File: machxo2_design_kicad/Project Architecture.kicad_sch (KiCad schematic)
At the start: 0 parts

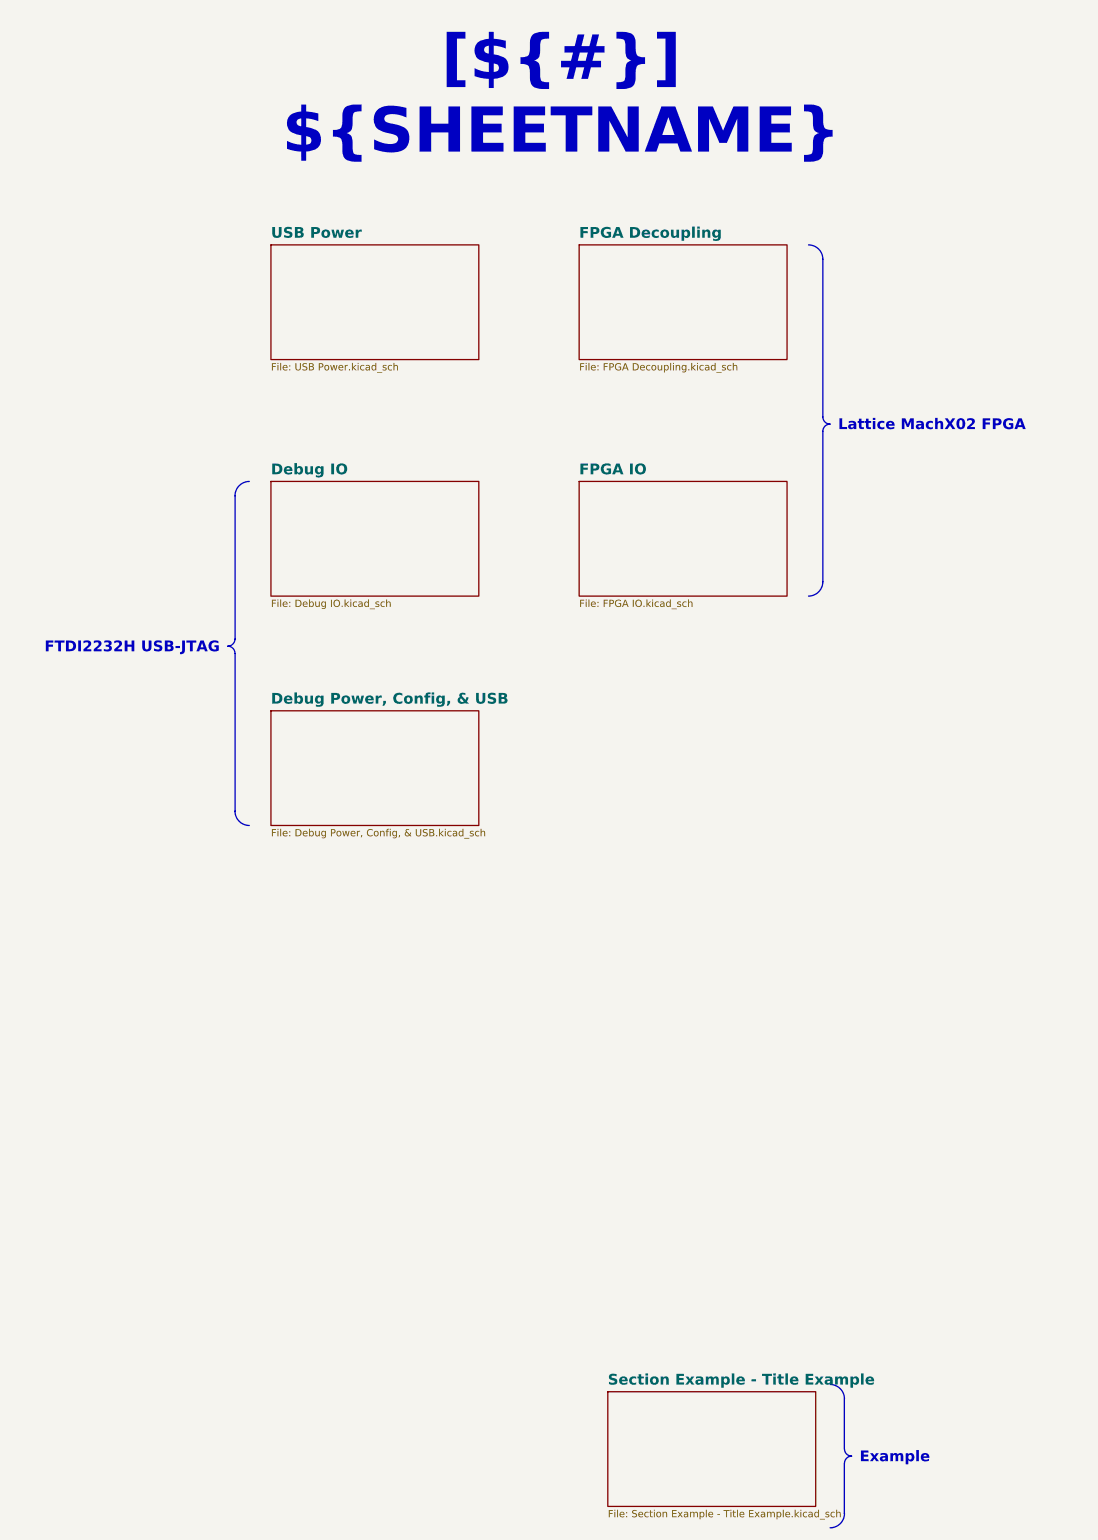
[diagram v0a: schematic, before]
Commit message: Prelimary schematic done. Need to create BOM and review.
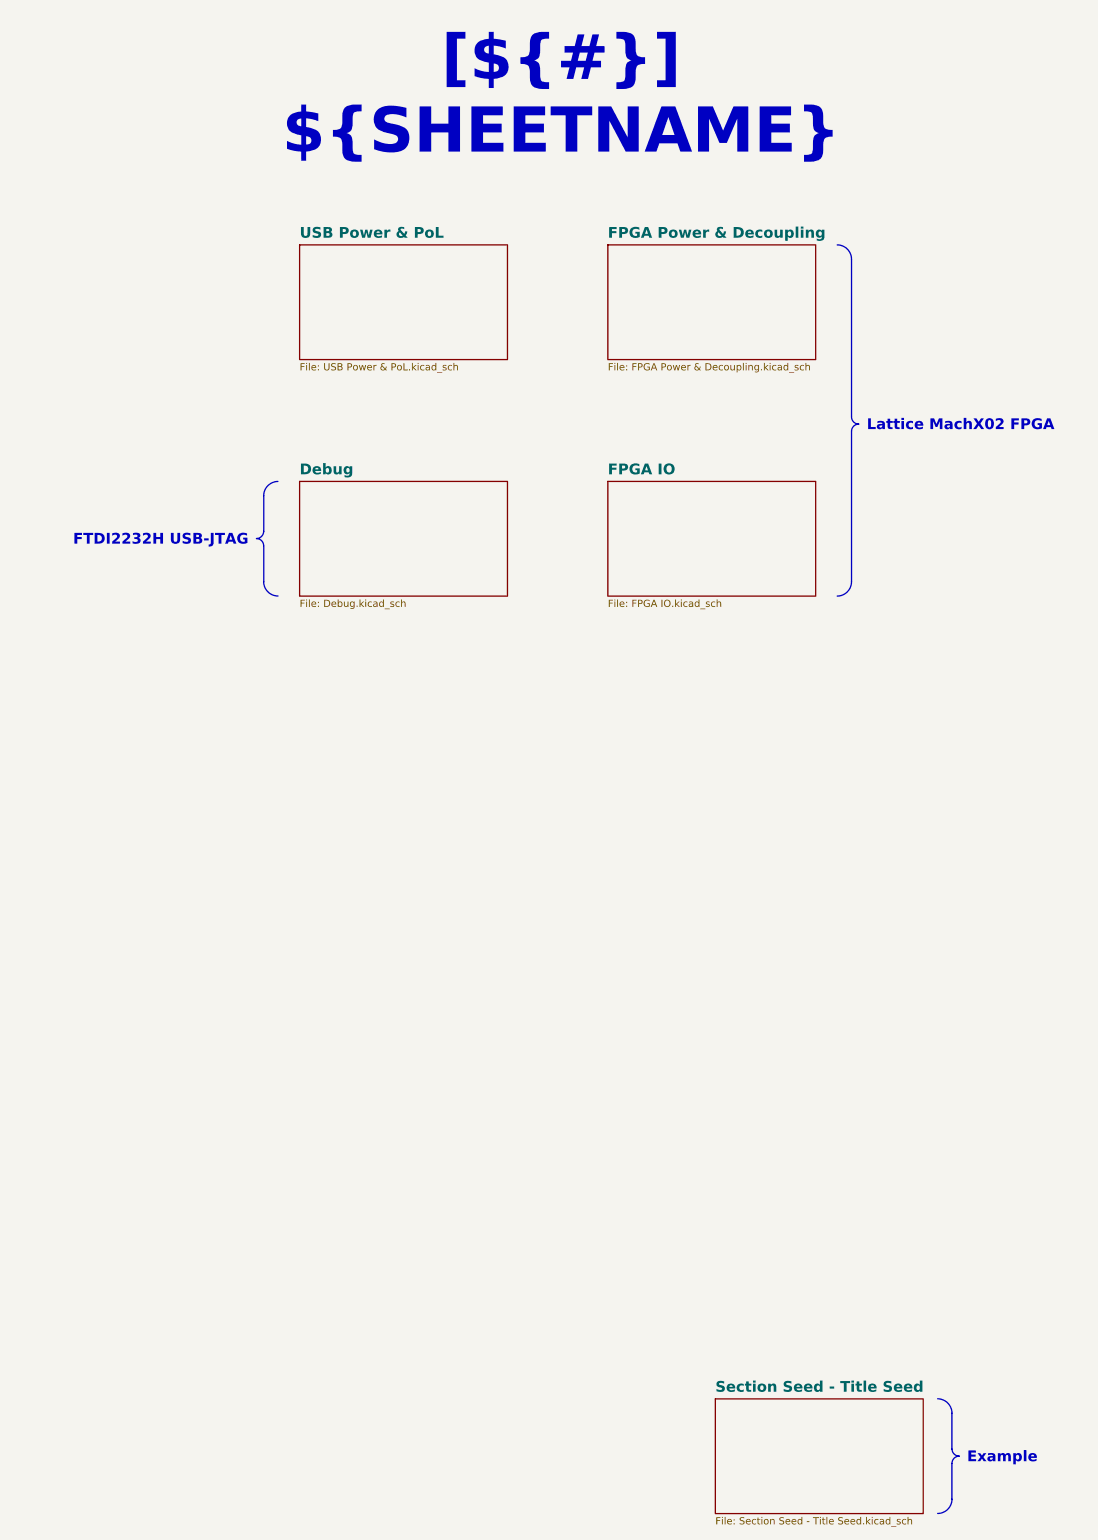
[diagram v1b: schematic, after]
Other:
- sheet Debug Power, Config, & USB renamed Debug
- sheet FPGA Decoupling renamed FPGA Power & Decoupling
- sheet Section Example - Title Example renamed Section Seed - Title Seed
- sheet USB Power renamed USB Power & PoL
- removed sheet Debug IO
- sheet Debug: file Debug Power, Config, & USB.kicad_sch -> Debug.kicad_sch
- sheet FPGA Power & Decoupling: file FPGA Decoupling.kicad_sch -> FPGA Power & Decoupling.kicad_sch
- sheet Section Seed - Title Seed: file Section Example - Title Example.kicad_sch -> Section Seed - Title Seed.kicad_sch
- sheet USB Power & PoL: file USB Power.kicad_sch -> USB Power & PoL.kicad_sch
